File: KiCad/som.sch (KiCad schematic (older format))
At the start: 39 parts, among them T2 BSS138APW, T4 BSS138APW, T5 BSS138APW

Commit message: Move ethernet connector closet to the edge. Loclib
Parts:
- FB2: footprint antmicro-footprints:0805-cap -> jetson-nano-baseboard-footprints:0805-cap; symbol Device:Ferrite_Bead_Small -> jetson-nano-baseboard:Ferrite_Bead_Small
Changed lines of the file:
@@
 	14600 2050 14800 2050
 $Comp
-L Device:Ferrite_Bead_Small FB?
+L jetson-nano-baseboard:Ferrite_Bead_Small FB?
 U 1 1 618512B9
 P 14500 2050
@@
 F 0 "FB2" V 14375 2050 50  0000 C CNN
 F 1 "742792022 " V 14625 2050 50  0000 C CNN
-F 2 "antmicro-footprints:0805-cap" V 14430 2050 50  0001 C CNN
+F 2 "jetson-nano-baseboard-footprints:0805-cap" V 14430 2050 50  0001 C CNN
 F 3 "~" H 14500 2050 50  0001 C CNN
 	1    14500 2050

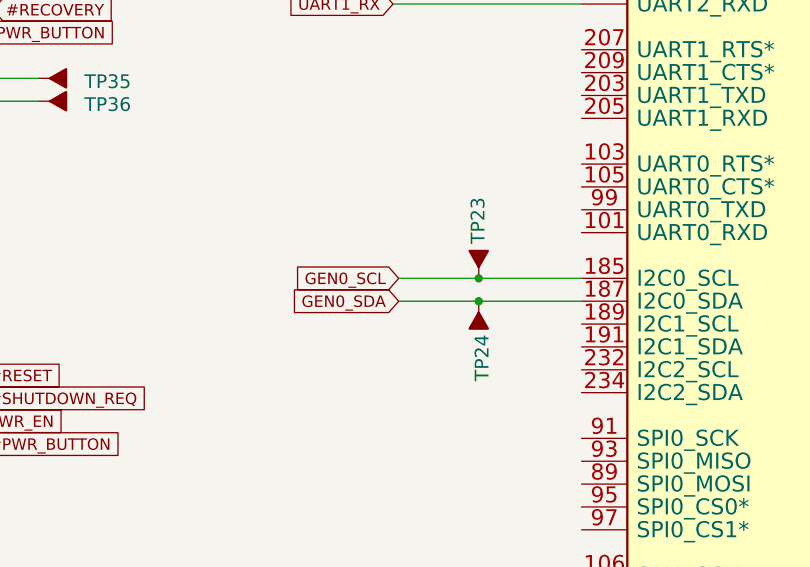
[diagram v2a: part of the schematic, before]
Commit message: Change I2C mux
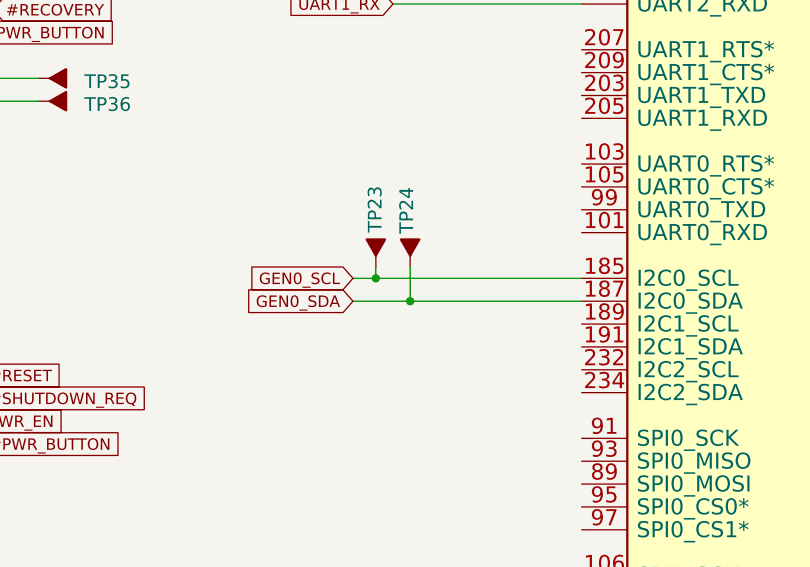
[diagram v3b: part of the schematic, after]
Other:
- moved on the sheet: TP23, TP24
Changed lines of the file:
@@
 L jetson-nano-baseboard:Testpad TP23
 U 1 1 5E710402
-P 6825 2600
-F 0 "TP23" V 6787 2905 60  0000 R TNN
-F 1 "~" H 6825 2600 50  0001 C CNN
-F 2 "jetson-nano-baseboard-footprints:TP-R-1.5" H 6825 2600 50  0001 C CNN
-F 3 "" H 6825 2600 50  0001 C CNN
-F 4 "N/A" H -16205 -862 50  0001 C CNN "MPN"
-F 5 "N/A" H -16205 -862 50  0001 C CNN "Manufacturer"
-	1    6825 2600
+P 6375 2550
+F 0 "TP23" V 6337 2855 60  0000 R TNN
+F 1 "~" H 6375 2550 50  0001 C CNN
+F 2 "jetson-nano-baseboard-footprints:TP-R-1.5" H 6375 2550 50  0001 C CNN
+F 3 "" H 6375 2550 50  0001 C CNN
+F 4 "N/A" H -16655 -912 50  0001 C CNN "MPN"
+F 5 "N/A" H -16655 -912 50  0001 C CNN "Manufacturer"
+	1    6375 2550
 	1    0    0    -1
 $EndComp
@@
 L jetson-nano-baseboard:Testpad TP24
 U 1 1 5E710401
-P 6825 2800
-F 0 "TP24" V 6775 3100 60  0000 R TNN
-F 1 "~" H 6825 2800 50  0001 C CNN
-F 2 "jetson-nano-baseboard-footprints:TP-R-1.5" H 6825 2800 50  0001 C CNN
-F 3 "" H 6825 2800 50  0001 C CNN
-F 4 "N/A" H -16205 -762 50  0001 C CNN "MPN"
-F 5 "N/A" H -16205 -762 50  0001 C CNN "Manufacturer"
-	1    6825 2800
-	-1   0    0    1
+P 6525 2550
+F 0 "TP24" V 6475 2850 60  0000 R TNN
+F 1 "~" H 6525 2550 50  0001 C CNN
+F 2 "jetson-nano-baseboard-footprints:TP-R-1.5" H 6525 2550 50  0001 C CNN
+F 3 "" H 6525 2550 50  0001 C CNN
+F 4 "N/A" H -16505 -1012 50  0001 C CNN "MPN"
+F 5 "N/A" H -16505 -1012 50  0001 C CNN "Manufacturer"
+	1    6525 2550
+	1    0    0    -1
 $EndComp
 $Comp
@@
 	7275 5950 6450 5950
 Wire Wire Line
-	7275 2650 6825 2650
-Wire Wire Line
-	6475 2750 6825 2750
-Wire Wire Line
 	7275 1350 6450 1350
 Wire Wire Line
@@
 Text GLabel 6700 6700 0    50   Input ~ 0
 \PEWAKE_3V3
-Connection ~ 6825 2750
-Wire Wire Line
-	6825 2750 7275 2750
-Connection ~ 6825 2650
-Wire Wire Line
-	6825 2650 6475 2650
-Text GLabel 6475 2650 0    50   Input ~ 0
+Text GLabel 6275 2650 0    50   Input ~ 0
 GEN0_SCL
-Text GLabel 6475 2750 0    50   Input ~ 0
+Text GLabel 6275 2750 0    50   Input ~ 0
 GEN0_SDA
 Text GLabel 4850 1375 2    50   Input ~ 0
@@
 	1    0    0    -1
 $EndComp
+Wire Wire Line
+	6375 2600 6375 2650
+Wire Wire Line
+	6275 2650 6375 2650
+Wire Wire Line
+	6275 2750 6525 2750
+Connection ~ 6375 2650
+Wire Wire Line
+	6375 2650 7275 2650
+Wire Wire Line
+	6525 2600 6525 2750
+Connection ~ 6525 2750
+Wire Wire Line
+	6525 2750 7275 2750
 $EndSCHEMATC

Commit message: Change fan design to match Nvidia. Change user button and led pins
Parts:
- renumbered TP35 to TP13, TP36 to TP14
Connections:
- net USR_BUTTON: no longer M1.208 (GPIO08), TP14.1 (P)
- net USR_LED: no longer M1.230 (GPIO14), TP13.1 (P)
- net #MOD_SLEEP: no longer names the net of M1.178 (MOD_SLEEP*)
- new net FAN_PWM: M1.230 (GPIO14), TP13.1 (P)
- new net FAN_TACH: M1.208 (GPIO08), TP14.1 (P)
- no-connect marks 0 -> 1
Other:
- moved on the sheet: TP13, TP14
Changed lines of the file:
@@
 Text Label 750  8450 0    60   ~ 0
 BT_M2_EN
-Text Label 3925 1875 0    60   ~ 0
-USR_BUTTON
 Text Label 2030 6162 0    70   ~ 0
 2309413-1
@@
 Text Label 2055 11062 0    70   ~ 0
 2309413-1
-Text Label 15100 5025 2    60   ~ 0
-USR_LED
-Text Label 3925 1775 0    60   ~ 0
-USR_LED
-Text Label 13225 7675 2    60   ~ 0
-USR_BUTTON
 Text Label 3925 1275 0    60   ~ 0
 PMIC_BBAT
@@
 $EndComp
 $Comp
-L jetson-nano-baseboard:Testpad TP35
-U 1 1 5E710404
-P 4950 1775
-F 0 "TP35" V 5000 1925 60  0000 L BNN
-F 1 "~" H 4950 1775 50  0001 C CNN
-F 2 "jetson-nano-baseboard-footprints:TP-R-1.5" H 4950 1775 50  0001 C CNN
-F 3 "" H 4950 1775 50  0001 C CNN
-F 4 "N/A" H -15080 -1087 50  0001 C CNN "MPN"
-F 5 "N/A" H -15080 -1087 50  0001 C CNN "Manufacturer"
-	1    4950 1775
-	0    1    1    0
-$EndComp
-$Comp
-L jetson-nano-baseboard:Testpad TP36
-U 1 1 5E710403
-P 4950 1875
-F 0 "TP36" V 5000 2025 60  0000 L BNN
-F 1 "~" H 4950 1875 50  0001 C CNN
-F 2 "jetson-nano-baseboard-footprints:TP-R-1.5" H 4950 1875 50  0001 C CNN
-F 3 "" H 4950 1875 50  0001 C CNN
-F 4 "N/A" H -15080 -1087 50  0001 C CNN "MPN"
-F 5 "N/A" H -15080 -1087 50  0001 C CNN "Manufacturer"
-	1    4950 1875
-	0    1    1    0
-$EndComp
-$Comp
 L jetson-nano-baseboard:Testpad TP23
 U 1 1 5E710402
@@
 	1275 10050 1875 10050
 Wire Wire Line
-	1275 10550 1875 10550
-Wire Wire Line
 	1350 10650 1875 10650
 Wire Wire Line
@@
 Wire Wire Line
 	3850 1075 4825 1075
-Wire Wire Line
-	3850 1775 4900 1775
-Wire Wire Line
-	3850 1875 4900 1875
 Wire Wire Line
 	14800 2200 14800 2050
@@
 Text GLabel 6450 1450 0    50   Input ~ 0
 UART1_RX
-Text GLabel 1275 10550 0    50   Input ~ 0
-#MOD_SLEEP
 Text GLabel 1350 10650 0    50   Input ~ 0
 VSYNC_CAM1_1
@@
 Wire Wire Line
 	6525 2750 7275 2750
+Wire Wire Line
+	3850 1775 4775 1775
+Wire Wire Line
+	3850 1875 4750 1875
+Text GLabel 4775 1775 2    50   Output ~ 0
+FAN_PWM
+Text GLabel 4750 1875 2    50   Input ~ 0
+FAN_TACH
+Text Label 4725 5075 0    60   ~ 0
+USR_BUTTON
+Text Label 4725 4975 0    60   ~ 0
+USR_LED
+$Comp
+L jetson-nano-baseboard:Testpad TP13
+U 1 1 5E710404
+P 4575 2875
+F 0 "TP13" V 4575 2975 60  0000 L BNN
+F 1 "~" H 4575 2875 50  0001 C CNN
+F 2 "jetson-nano-baseboard-footprints:TP-R-1.5" H 4575 2875 50  0001 C CNN
+F 3 "" H 4575 2875 50  0001 C CNN
+F 4 "N/A" H -15455 13  50  0001 C CNN "MPN"
+F 5 "N/A" H -15455 13  50  0001 C CNN "Manufacturer"
+	1    4575 2875
+	0    -1   1    0
+$EndComp
+$Comp
+L jetson-nano-baseboard:Testpad TP14
+U 1 1 5E710403
+P 4575 2975
+F 0 "TP14" V 4575 3075 60  0000 L BNN
+F 1 "~" H 4575 2975 50  0001 C CNN
+F 2 "jetson-nano-baseboard-footprints:TP-R-1.5" H 4575 2975 50  0001 C CNN
+F 3 "" H 4575 2975 50  0001 C CNN
+F 4 "N/A" H -15455 13  50  0001 C CNN "MPN"
+F 5 "N/A" H -15455 13  50  0001 C CNN "Manufacturer"
+	1    4575 2975
+	0    -1   1    0
+$EndComp
+Wire Wire Line
+	4650 4975 5700 4975
+Wire Wire Line
+	4650 5075 5700 5075
+Text GLabel 4625 2875 2    50   Input ~ 0
+FAN_PWM
+Text GLabel 4625 2975 2    50   Input ~ 0
+FAN_TACH
+Text GLabel 15100 5025 2    50   Input ~ 0
+USR_LED
+Text GLabel 13225 7675 2    50   Output ~ 0
+USR_BUTTON
+NoConn ~ 1875 10550
 $EndSCHEMATC

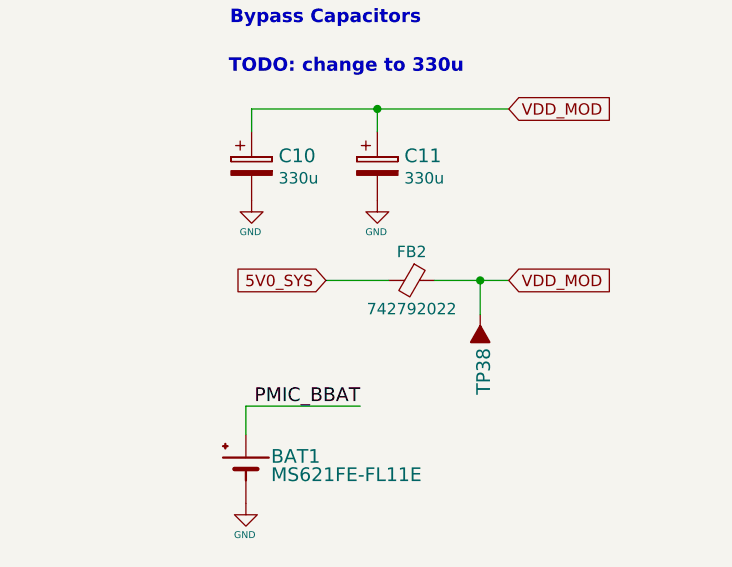
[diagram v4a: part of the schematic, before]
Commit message: 742792022  -> 74279221100
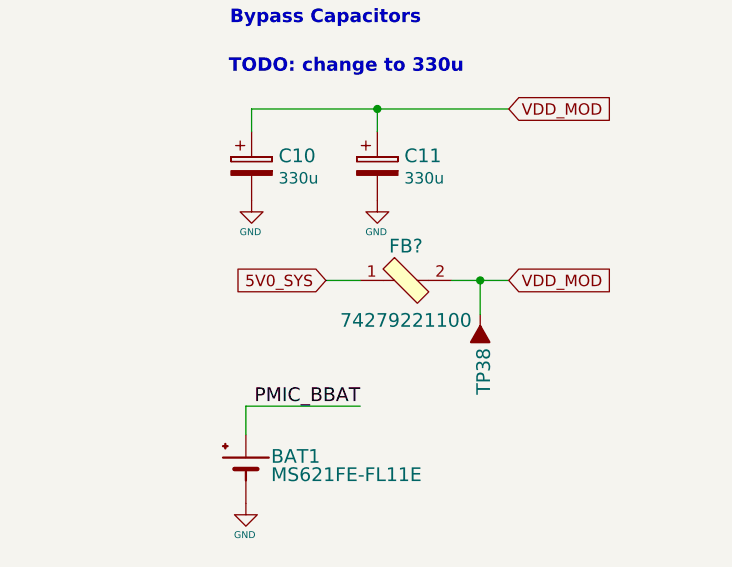
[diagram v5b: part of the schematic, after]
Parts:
- removed FB2: 742792022, jetson-nano-baseboard-footprints:0805-cap, symbol jetson-nano-baseboard:Ferrite_Bead_Small
- added FB?: 74279221100, antmicro-footprints:1206-res, symbol antmicroFerriteBeadsandChips:74279221100
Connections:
- net 5V0_SYS: now also FB?.1
- net VDD_MOD: now also FB?.2
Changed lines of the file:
@@
 Wire Wire Line
 	14650 5200 14750 5200
-Wire Wire Line
-	14125 2050 14400 2050
-Wire Wire Line
-	14600 2050 14800 2050
-$Comp
-L jetson-nano-baseboard:Ferrite_Bead_Small FB?
-U 1 1 618512B9
-P 14500 2050
-AR Path="/608DC6E9/618512B9" Ref="FB?"  Part="1"
-AR Path="/610ACCAB/618512B9" Ref="FB2"  Part="1"
-F 0 "FB2" V 14375 2050 50  0000 C CNN
-F 1 "742792022 " V 14625 2050 50  0000 C CNN
-F 2 "jetson-nano-baseboard-footprints:0805-cap" V 14430 2050 50  0001 C CNN
-F 3 "~" H 14500 2050 50  0001 C CNN
-	1    14500 2050
-	0    1    1    0
-$EndComp
 $Comp
 L jetson-nano-baseboard:SPACER SP6
@@
 USR_BUTTON
 NoConn ~ 1875 10550
+Wire Wire Line
+	14125 2050 14275 2050
+$Comp
+L antmicroFerriteBeadsandChips:74279221100 FB?
+U 1 1 62552116
+P 14475 2050
+F 0 "FB?" H 14475 2200 60  0000 C CNN
+F 1 "74279221100" H 14475 1875 60  0000 C CNN
+F 2 "antmicro-footprints:1206-res" H 14675 2250 60  0001 L CNN
+F 3 "https://www.we-online.com/catalog/datasheet/74279221100.pdf" H 14675 2350 60  0001 L CNN
+F 4 "74279221100" H 14675 2550 60  0001 L CNN "MPN"
+F 5 "Wurth Electronic" H 14675 3150 60  0001 L CNN "Manufacturer"
+	1    14475 2050
+	1    0    0    -1
+$EndComp
+Wire Wire Line
+	14675 2050 14800 2050
 $EndSCHEMATC

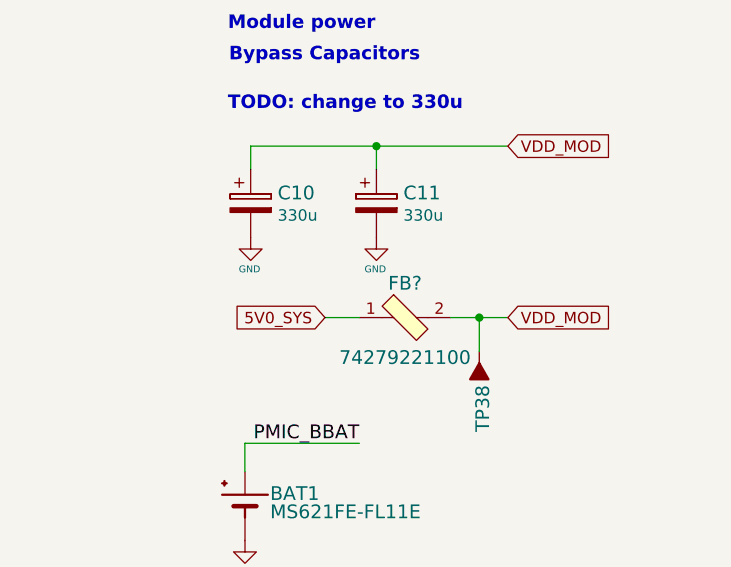
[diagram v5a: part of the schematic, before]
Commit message: Annotate parts
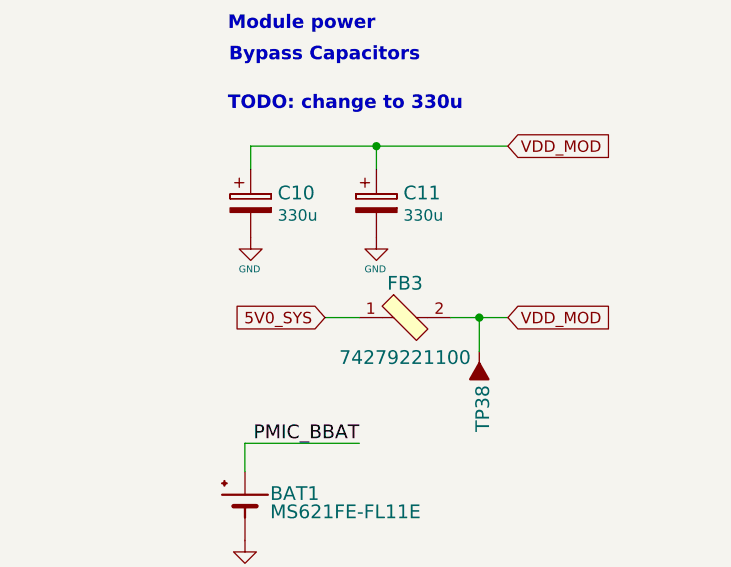
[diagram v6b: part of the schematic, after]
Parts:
- gave numbers to parts that had none: 1
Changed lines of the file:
@@
 	14125 2050 14275 2050
 $Comp
-L antmicroFerriteBeadsandChips:74279221100 FB?
+L antmicroFerriteBeadsandChips:74279221100 FB3
 U 1 1 62552116
 P 14475 2050
-F 0 "FB?" H 14475 2200 60  0000 C CNN
+F 0 "FB3" H 14475 2200 60  0000 C CNN
 F 1 "74279221100" H 14475 1875 60  0000 C CNN
 F 2 "antmicro-footprints:1206-res" H 14675 2250 60  0001 L CNN

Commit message: Saving changes for later work
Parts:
- removed J10: ~, jetson-nano-baseboard-footprints:PCA-10, symbol jetson-nano-baseboard:ADAM-TECH_PCA-10
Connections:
- net UART1_RX: now also M1_4.205 (UART1_RXD); no longer M1_4.238 (UART2_RXD)
- net UART1_TX: now also M1_4.203 (UART1_TXD); no longer M1_4.236 (UART2_TXD)
- net CAN_RX: now reaches M1.143 ((CAN_RX)RSVD)
- net CAN_TX: now reaches M1.145 ((CAN_TX)RSVD)
- net I2C1_SCL: now reaches M1_4.189 (I2C1_SCL)
- net I2C1_SDA: now reaches M1_4.191 (I2C1_SDA)
- net SPI0_MOSI: now reaches M1_4.89 (SPI0_MOSI)
- net SPI0_SCK: now reaches M1_4.91 (SPI0_SCK)
- net SPI0_MISO: now reaches M1_4.93 (SPI0_MISO)
- net SPI0_CS#: now reaches M1_4.95 (SPI0_CS0*)
- new net UART2_RX: M1_4.238 (UART2_RXD)
- new net UART2_TX: M1_4.236 (UART2_TXD)
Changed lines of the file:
@@
 Comment4 ""
 $EndDescr
-Text Label 6450 5950 0    60   ~ 0
-USB2_D_P
-Text Label 6450 5850 0    60   ~ 0
-USB2_D_N
 Text Notes 10055 10037 0    96   ~ 0
 Mechanical model
@@
 Text Label 14275 2600 2    60   ~ 0
 PMIC_BBAT
-Text Label 10525 2075 0    60   ~ 0
-PCIE1_RX0_N
-Text Label 10525 1975 0    60   ~ 0
-PCIE1_RX0_P
-Text Label 10525 1875 0    60   ~ 0
-PCIE1_TX0_N
-Text Label 10525 1775 0    60   ~ 0
-PCIE1_TX0_P
-Text Label 10525 1675 0    60   ~ 0
-PCIE1_CLK_N
-Text Label 10525 1575 0    60   ~ 0
-PCIE1_CLK_P
-Text Label 10525 1475 0    60   ~ 0
-PCIE1_CLKREQ
-Text Label 10525 1375 0    60   ~ 0
-PCIE1_RST
 Text Notes 2669 49363 0    60   ~ 0
 Text
@@
 Text GLabel 12800 4025 1    50   Input ~ 0
 5V0_SYS
-Text GLabel 11300 1125 1    50   Input ~ 0
-3V3_SYS
 Text GLabel 14125 2050 0    50   Input ~ 0
 5V0_SYS
@@
 F 3 "" H 13775 3025 70  0001 C CNN
 	1    13775 3025
-	1    0    0    -1
-$EndComp
-$Comp
-L jetson-nano-baseboard:GND #GND_055
-U 1 1 5E710414
-P 11300 2250
-F 0 "#GND_055" H 11300 2250 20  0001 C CNN
-F 1 "GND" H 11295 2112 30  0000 C CNN
-F 2 "" H 11300 2250 70  0001 C CNN
-F 3 "" H 11300 2250 70  0001 C CNN
-	1    11300 2250
 	1    0    0    -1
 $EndComp
@@
 F 5 "Seiko" H -2705 -7037 50  0001 C CNN "Manufacturer"
 	1    13775 2825
-	1    0    0    -1
-$EndComp
-$Comp
-L jetson-nano-baseboard:ADAM-TECH_PCA-10 J10
-U 1 1 5E7103EF
-P 11650 1675
-F 0 "J10" H 11650 975 60  0000 L BNN
-F 1 "~" H 11650 1675 50  0001 C CNN
-F 2 "jetson-nano-baseboard-footprints:PCA-10" H 11650 1675 50  0001 C CNN
-F 3 "" H 11650 1675 50  0001 C CNN
-F 4 "PCA-10" H -9930 -4187 50  0001 C CNN "MPN"
-F 5 "Adam Tech" H -9930 -4187 50  0001 C CNN "Manufacturer"
-	1    11650 1675
 	1    0    0    -1
 $EndComp
@@
 	15100 9225 15100 9425
 Wire Wire Line
-	11450 1275 11300 1275
-Wire Wire Line
-	11450 1375 10525 1375
-Wire Wire Line
-	11450 1475 10525 1475
-Wire Wire Line
-	10525 1575 11450 1575
-Wire Wire Line
-	10525 1675 11450 1675
-Wire Wire Line
-	10525 1775 11450 1775
-Wire Wire Line
-	10525 1875 11450 1875
-Wire Wire Line
-	10525 1975 11450 1975
-Wire Wire Line
-	10525 2075 11450 2075
-Wire Wire Line
-	11450 2175 11300 2175
-Wire Wire Line
-	11300 2175 11300 2250
-Wire Wire Line
-	11300 1125 11300 1275
-Wire Wire Line
 	11825 5025 11975 5025
 Wire Wire Line
@@
 	7275 5650 6825 5650
 Wire Wire Line
-	6450 5850 7275 5850
-Wire Wire Line
-	7275 5950 6450 5950
+	6825 5850 7275 5850
+Wire Wire Line
+	7275 5950 6825 5950
 Wire Wire Line
 	7275 1350 6450 1350
@@
 ENET_TRD0_N
 Text GLabel 6450 1350 0    50   Input ~ 0
-UART1_TX
+UART2_TX
 Text GLabel 6450 1450 0    50   Input ~ 0
-UART1_RX
+UART2_RX
 Text GLabel 1350 10650 0    50   Input ~ 0
 VSYNC_CAM1_1
@@
 Wire Wire Line
 	14675 2050 14800 2050
+Text GLabel 6825 5850 0    50   Input ~ 0
+USB2_D_N
+Text GLabel 6825 5950 0    50   Input ~ 0
+USB2_D_P
+Text GLabel 6275 2850 0    50   Input ~ 0
+I2C1_SCL
+Text GLabel 6275 2950 0    50   Input ~ 0
+I2C1_SDA
+Wire Wire Line
+	6275 2850 7275 2850
+Wire Wire Line
+	7275 2950 6275 2950
+Text GLabel 1275 10250 0    50   Input ~ 0
+CAN_RX
+Text GLabel 1275 10350 0    50   Input ~ 0
+CAN_TX
+Wire Wire Line
+	1275 10250 1875 10250
+Wire Wire Line
+	1875 10350 1275 10350
+Wire Wire Line
+	7275 1850 6450 1850
+Wire Wire Line
+	7275 1950 6450 1950
+Text GLabel 6450 1850 0    50   Input ~ 0
+UART1_TX
+Text GLabel 6450 1950 0    50   Input ~ 0
+UART1_RX
+Wire Wire Line
+	7275 3350 6450 3350
+Wire Wire Line
+	7275 3450 6450 3450
+Wire Wire Line
+	7275 3550 6450 3550
+Wire Wire Line
+	7275 3650 6450 3650
+Text GLabel 6450 3650 0    50   Input ~ 0
+SPI0_CS#
+Text GLabel 6450 3550 0    50   Input ~ 0
+SPI0_MOSI
+Text GLabel 6450 3450 0    50   Input ~ 0
+SPI0_MISO
+Text GLabel 6450 3350 0    50   Input ~ 0
+SPI0_SCK
 $EndSCHEMATC

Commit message: Loclib
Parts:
- FB3: footprint antmicro-footprints:1206-res -> jetson-nano-baseboard-footprints:1206-res; symbol antmicroFerriteBeadsandChips:74279221100 -> jetson-nano-baseboard:74279221100
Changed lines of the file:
@@
 	14125 2050 14275 2050
 $Comp
-L antmicroFerriteBeadsandChips:74279221100 FB3
+L jetson-nano-baseboard:74279221100 FB3
 U 1 1 62552116
 P 14475 2050
 F 0 "FB3" H 14475 2200 60  0000 C CNN
 F 1 "74279221100" H 14475 1875 60  0000 C CNN
-F 2 "antmicro-footprints:1206-res" H 14675 2250 60  0001 L CNN
+F 2 "jetson-nano-baseboard-footprints:1206-res" H 14675 2250 60  0001 L CNN
 F 3 "https://www.we-online.com/catalog/datasheet/74279221100.pdf" H 14675 2350 60  0001 L CNN
 F 4 "74279221100" H 14675 2550 60  0001 L CNN "MPN"
